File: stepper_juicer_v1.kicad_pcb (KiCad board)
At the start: 2 copper layers, 62 parts, among them J1 Conn_01x06_Pin, J2 Barrel_Jack_Switch, J3 Conn_01x04_Pin, J4 Conn_01x06_Pin, Q1 NMOS, Q2 NMOS, Q3 NMOS, Q4 NMOS, Q5 NMOS, Q6 NMOS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

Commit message: Finish design
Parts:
- removed C1, C11, C14, C8: 1uF 50V, Capacitor_SMD:C_0402_1005Metric
- added G***: LOGO, _custom_library:Peanut, F.Cu at (106.2, 82.2)
- added H1: M3 Pad, MountingHole:MountingHole_3.2mm_M3_Pad, F.Cu at (104.5, 75.0)
- added H2: M3 Pad, MountingHole:MountingHole_3.2mm_M3_Pad, F.Cu at (104.5, 115.0)
- added H3: M3 Pad, MountingHole:MountingHole_3.2mm_M3_Pad, F.Cu at (135.5, 115.0)
- added TP1: TestPoint, TestPoint:TestPoint_Pad_D1.0mm, B.Cu at (125.2, 82.0)
- added TP2: TestPoint, TestPoint:TestPoint_Pad_D1.0mm, B.Cu at (119.1, 84.0)
- added TP3: TestPoint, TestPoint:TestPoint_Pad_D1.0mm, B.Cu at (131.2, 82.0)
- C12, C15, C6, C9: footprint Capacitor_SMD:C_0402_1005Metric -> Capacitor_SMD:C_0805_2012Metric
- D5, D6, D7, D8: value 100V 2A -> 100V 200mA; footprint Diode_SMD:Nexperia_CFP3_SOD-123W -> Diode_SMD:D_SOD-323F
- R12, R15, R18, R9: footprint Resistor_SMD:R_0805_2012Metric -> Resistor_SMD:R_0603_1608Metric
- moved R19 81.2 mm to (112.6, 116.4)
- moved R16 77.5 mm to (112.7, 83.7)
- moved R18 77.3 mm to (116.5, 113.4), turned to 90 degrees
- moved D8 76.6 mm to (117.5, 111.0)
- moved C15 76.2 mm to (115.3, 117.2), turned to -90 degrees
- moved R13 76.0 mm to (112.5, 105.6)
- moved C9 74.7 mm to (115.2, 106.4), turned to -90 degrees
- moved D6 74.7 mm to (117.4, 100.2)
- moved R15 73.6 mm to (116.6, 80.8), turned to 90 degrees
- moved D5 71.6 mm to (117.5, 89.2)
- moved C6 71.5 mm to (115.3, 95.5), turned to -90 degrees
- moved R17 71.4 mm to (121.8, 81.9), turned to -90 degrees
- moved R20 71.3 mm to (121.7, 114.5), turned to -90 degrees
- moved R11 70.8 mm to (112.6, 94.7)
- moved U3 70.7 mm to (129.8, 111.5)
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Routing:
- net +48V: track 0.00 -> 38.1 mm, vias 0 -> 27
- net /A_IN-: track 0.00 -> 30.6 mm, vias 0 -> 2
- net /B_IN-: track 0.00 -> 30.1 mm, vias 0 -> 2
- net /B_IN+: track 0.00 -> 29.5 mm
- net /A_IN+: track 0.00 -> 28.5 mm
- net +12V: track 0.00 -> 5.52 mm, vias 0 -> 23
- net /A_DRIVE-: track 0.00 -> 4.69 mm
- net /B_DRIVE+: track 0.00 -> 4.65 mm
- net GND: track 0.00 -> 4.56 mm, vias 0 -> 83
- net /B_DRIVE-: track 0.00 -> 4.55 mm
- net /A_DRIVE+: track 0.00 -> 4.51 mm
- net Net-(D9-K): track 0.00 -> 2.22 mm
- added copper zone on B.Cu, net +12V
- added copper zone on F.Cu, net +12V
- added copper zone on B.Cu, net +48V
- added copper zone on F.Cu, net +48V
- added copper zone on F.Cu, net /A_OUT+
- added copper zone on F.Cu, net /A_OUT-
- added copper zone on F.Cu, net /B_OUT+
- added copper zone on F.Cu, net /B_OUT-
- added copper zone on B.Cu, net GND
- added copper zone on F.Cu, net GND
- added copper zone on In1.Cu, net GND
- added copper zone on In2.Cu, net GND
- added copper zone on F.Cu, net Net-(D5-K)
- added copper zone on F.Cu, net Net-(D6-K)
- added copper zone on F.Cu, net Net-(D7-K)
- added copper zone on F.Cu, net Net-(D8-K)
- added copper zone on F.Cu, net Net-(Q1-G)
- added copper zone on F.Cu, net Net-(Q2-G)
- added copper zone on F.Cu, net Net-(Q3-G)
- added copper zone on F.Cu, net Net-(Q4-G)
- added copper zone on F.Cu, net Net-(Q5-G)
- added copper zone on F.Cu, net Net-(Q6-G)
- added copper zone on F.Cu, net Net-(Q7-G)
- added copper zone on F.Cu, net Net-(Q8-G)
- added copper zone on F.Cu, net Net-(U1-DRVH)
- added copper zone on F.Cu, net Net-(U1-DRVL)
- added copper zone on F.Cu, net Net-(U1-VB)
- added copper zone on F.Cu, net Net-(U2-DRVH)
- added copper zone on F.Cu, net Net-(U2-DRVL)
- added copper zone on F.Cu, net Net-(U2-VB)
- added copper zone on F.Cu, net Net-(U4-DRVH)
- added copper zone on F.Cu, net Net-(U4-DRVL)
- added copper zone on F.Cu, net Net-(U4-VB)
- added copper zone on F.Cu, net Net-(U5-DRVH)
- added copper zone on F.Cu, net Net-(U5-DRVL)
- added copper zone on F.Cu, net Net-(U5-VB)
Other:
- board outline added: 40 x 50 mm
- copper layers 2 -> 4
- board text added: "12V"
- board text added: "2-PHASE STEPPER DRIVER"
- board text added: "36-48V"
- board text added: "48V"
- board text added: "A.L."
- board text added: "B- B+ A- A+"
- board text added: "GND"

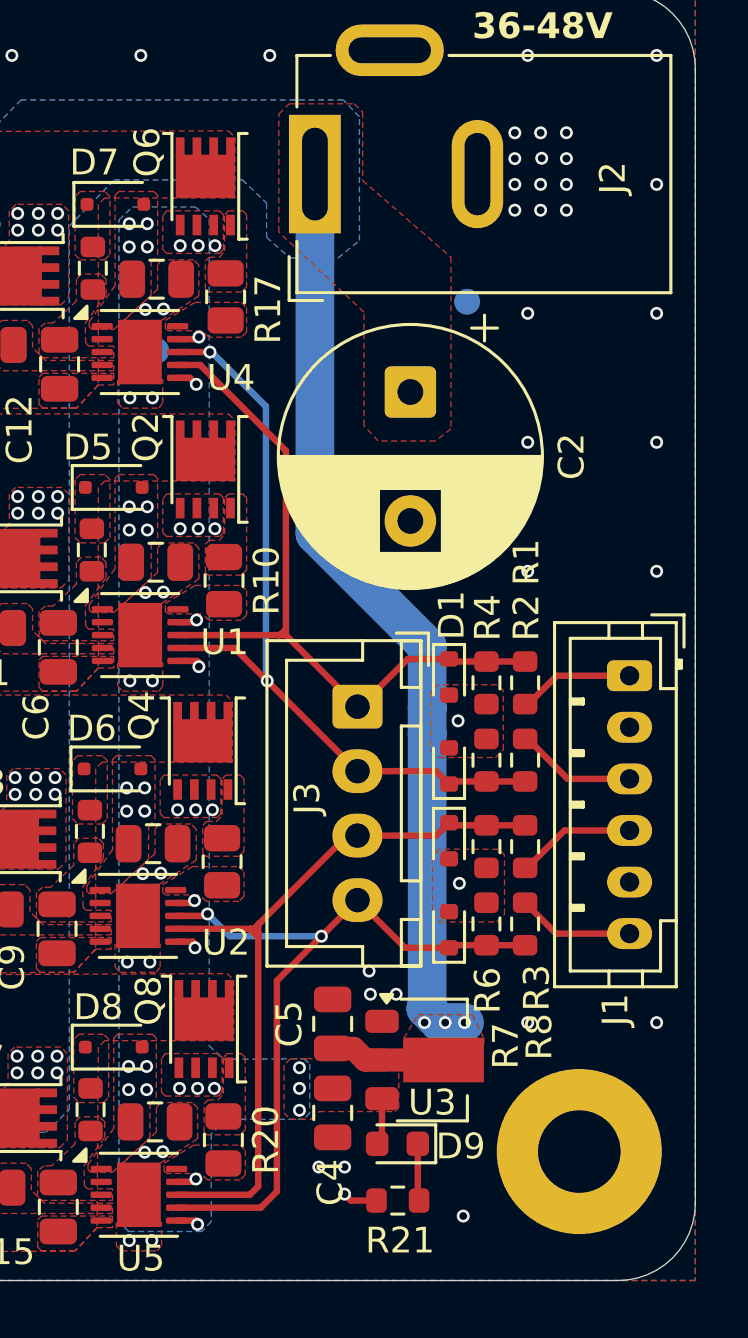
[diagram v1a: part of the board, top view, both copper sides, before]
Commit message: Add ground pin
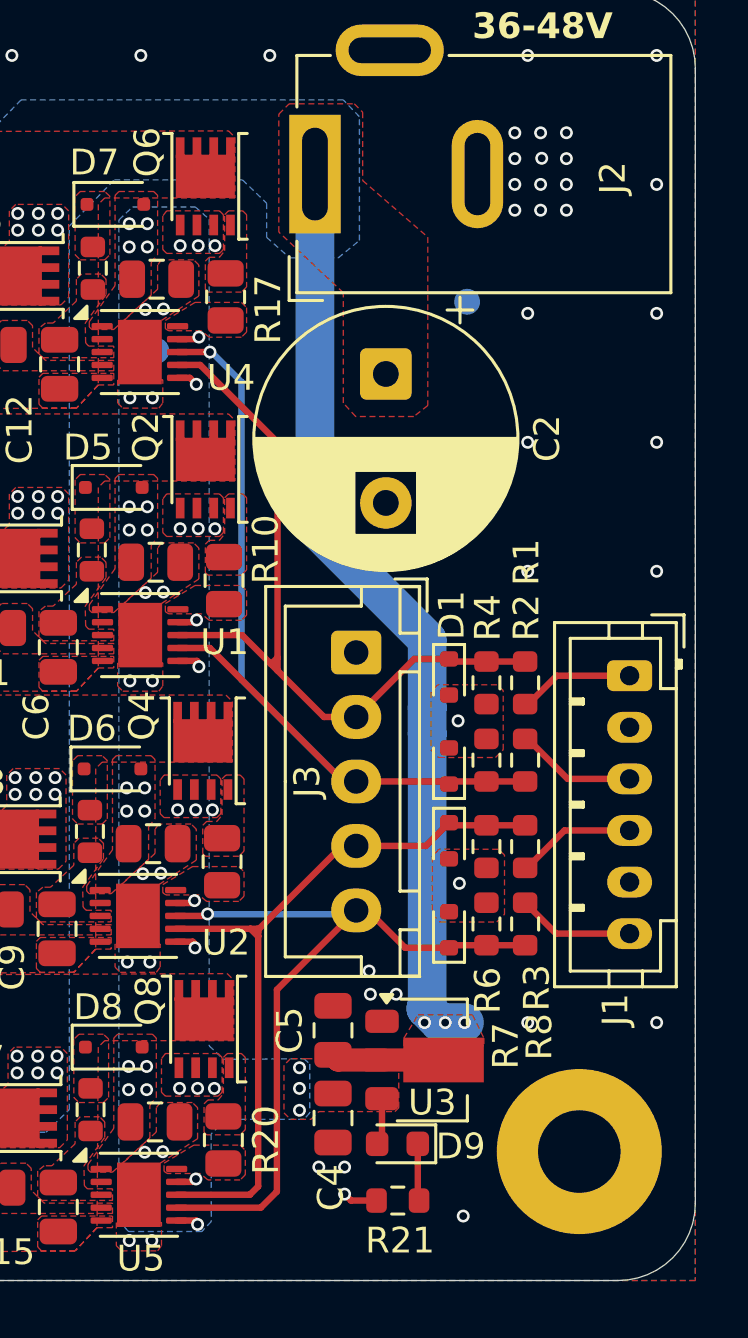
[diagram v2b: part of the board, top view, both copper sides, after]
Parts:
- J3: footprint Connector_JST:JST_XH_B4B-XH-A_1x04_P2.50mm_Vertical -> Connector_JST:JST_XH_B5B-XH-A_1x05_P2.50mm_Vertical
- moved J3 2.10 mm to (126.8, 95.7)
- moved C2 1.18 mm to (128.0, 84.8)
- moved C5 0.25 mm to (126.0, 110.3)
- moved C4 0.20 mm to (126.0, 113.7)
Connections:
- J3 pad 1: /A_IN+ -> GND
- J3 pad 2: /A_IN- -> /A_IN+
- J3 pad 3: /B_IN+ -> /A_IN-
- J3 pad 4: /B_IN- -> /B_IN+
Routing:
- net /A_IN-: track 30.6 -> 36.3 mm, vias 2 -> 1
- net /A_IN+: track 28.5 -> 30.2 mm
- net /B_IN-: track 30.1 -> 30.6 mm, vias 2 -> 1

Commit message: fixup! Add ground pin
Cosmetic change
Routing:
- net /B_IN-: track 30.6 -> 31.4 mm
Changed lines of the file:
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@@
 	)
 	(segment
-		(start 123.775 116.55)
-		(end 123.15 117.175)
-		(width 0.25)
-		(layer "F.Cu")
-		(net 15)
-	)
-	(segment
-		(start 123.15 117.175)
-		(end 119.8875 117.175)
+		(start 125.5 105.65)
+		(end 123.775 107.375)
 		(width 0.25)
 		(layer "F.Cu")
@@
 	(segment
 		(start 126.85 105.65)
-		(end 123.775 108.725)
+		(end 125.5 105.65)
 		(width 0.25)
 		(layer "F.Cu")
@@
 		(start 127.3 105.65)
 		(end 126.85 105.65)
+		(width 0.25)
+		(layer "F.Cu")
+		(net 15)
+	)
+	(segment
+		(start 123.15 117.175)
+		(end 119.8875 117.175)
+		(width 0.25)
+		(layer "F.Cu")
+		(net 15)
+	)
+	(segment
+		(start 123.775 107.375)
+		(end 123.775 116.55)
 		(width 0.25)
 		(layer "F.Cu")
@@
 	)
 	(segment
-		(start 123.775 108.725)
-		(end 123.775 116.55)
+		(start 123.775 116.55)
+		(end 123.15 117.175)
 		(width 0.25)
 		(layer "F.Cu")
